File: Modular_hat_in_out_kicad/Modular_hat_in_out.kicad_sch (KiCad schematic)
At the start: 35 parts, among them J1 Raspberry_Pi_2_3, U1 MCP3008, U2 LM324, U3 MCP3008, U4 MCP4728

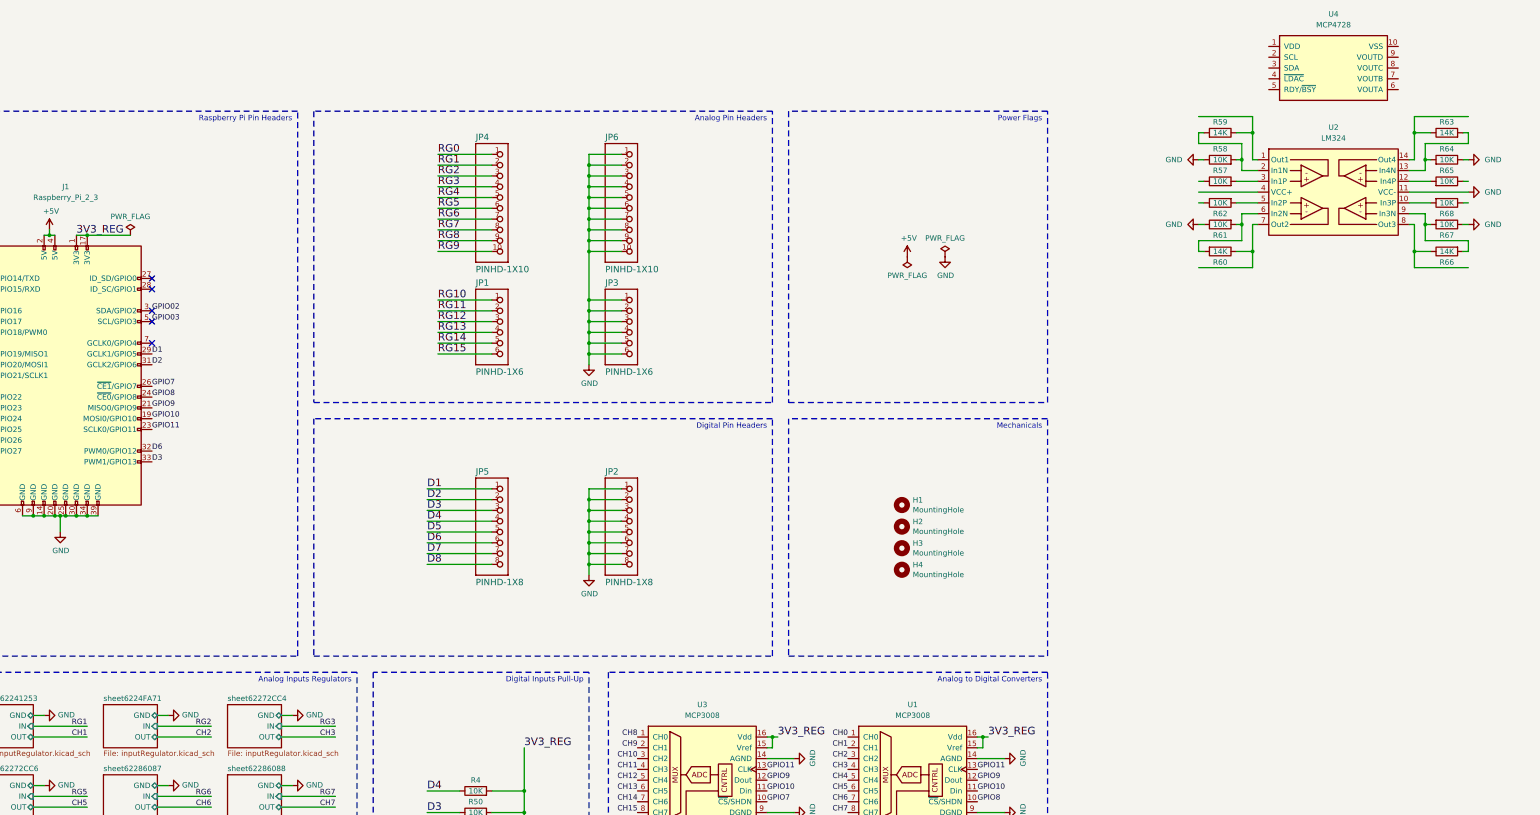
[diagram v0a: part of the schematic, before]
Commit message: [ADD] Connections and update configuration resistors
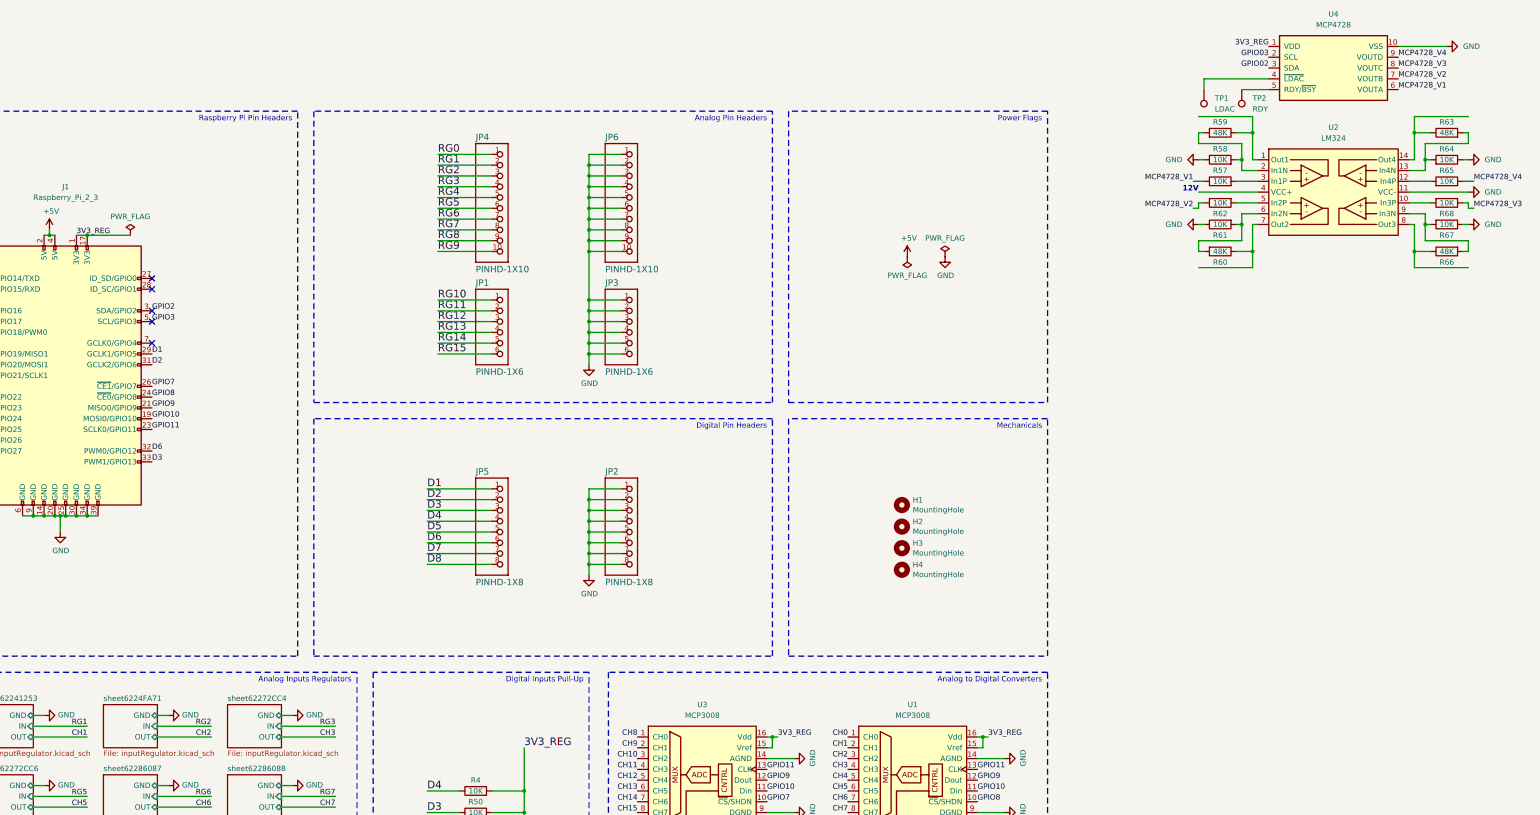
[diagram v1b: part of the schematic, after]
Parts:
- added TP1: LDAC, symbol Modular Shield:TestPoint
- added TP2: RDY, symbol Modular Shield:TestPoint
- R59, R60, R63, R66: value 14K -> 48K; symbol Modular Shield:R 14K -> Modular Shield:R 48K; LCSC C2930066 -> C227922
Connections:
- net 3V3_REG: now also U4.1 (VDD)
- net GND: now also U4.10 (VSS)
- net GPIO02: now also U4.3 (SDA); no longer J1.3 (SDA/GPIO2)
- net GPIO03: now also U4.2 (SCL); no longer J1.5 (SCL/GPIO3)
- net MCP4728_V3: now reaches R68.1
- net MCP4728_V3: now also U4.8 (VOUTC)
- net at U4.4 (~{LDAC}): now also TP1.1
- net at U4.5 (RDY/~{BSY}): now also TP2.1
- net MCP4728_V1: now reaches U4.6 (VOUTA)
- net MCP4728_V1: now also R57.1
- net MCP4728_V2: now reaches U4.7 (VOUTB)
- net MCP4728_V2: now also R62.1
- net MCP4728_V4: now reaches U4.9 (VOUTD)
- net MCP4728_V4: now also R65.1
- new net GPIO2: J1.3 (SDA/GPIO2)
- new net GPIO3: J1.5 (SCL/GPIO3)
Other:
- note added: "12V"

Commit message: [ADD] Update design and Schematics for 4 channels DAC seems OK
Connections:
- net OP0: now reaches R59.2, U2.1 (Out1)
- net OP4: now reaches R63.2, U2.14 (Out4)
- net OP3: now reaches R66.2, U2.8 (Out3)
- net OP2: now reaches R60.2, U2.7 (Out2)
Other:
- removed sheet sheet62241253
- removed sheet sheet6224FA71
- removed sheet sheet62272CC4
- removed sheet sheet62272CC5
- removed sheet sheet62272CC6
- removed sheet sheet62286087
- removed sheet sheet62286088
- removed sheet sheet62286089
- removed sheet sheet6229E4C7
- removed sheet sheet6229E4C8
- removed sheet sheet6229E4C9
- removed sheet sheet6229E4CA
- removed sheet sheet6229E4CB
- removed sheet sheet6229E4CC
- removed sheet sheet622B5734
- added sheet outputProtection (outputProtection.kicad_sch)
- moved on the sheet: TP1, TP2, U4

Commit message: [ADD] Schematics in progress
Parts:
- added C1, C3: 0.1uF, symbol Modular Shield:C
- added C2, C4: 10uF, symbol Modular Shield:C
- added JP7, JP8: PINHD-1X8, Modular Shield:1X08-BIG, symbol Modular Shield:PINHD-1X8
- added R73, R74, R75, R77, R78, R79, R80, R82, R84, R85, R86, R87: 10K, Modular Shield:R_0603_1608Metric, symbol Modular Shield:R 10K
- added R76, R81, R83, R88: 48K, Modular Shield:R_0603_1608Metric, symbol Modular Shield:R 48K
- added TP3: LDAC, symbol Modular Shield:TestPoint
- added TP4, TP5, TP6: RDY, symbol Modular Shield:TestPoint
- added U5: MCP4728, Package_SO:MSOP-10_3x3mm_P0.5mm, symbol Modular Shield:MCP4728
- added U6: LM324, symbol Modular Shield:LM324
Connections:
- net +5V: now also U4.1 (VDD), C1.1, C2.1, C3.1, C4.1, U5.1 (VDD)
- net 3V3_REG: now also R73.2, R74.1, R75.1, R82.2; no longer U4.1 (VDD)
- net GND: now also C1.2, C2.2, C3.2, C4.2, JP8.1, JP8.2, JP8.3, JP8.4, JP8.5, JP8.6, JP8.7, JP8.8, R77.1, R80.1, R84.1, R87.1, TP5.1, TP6.1, U5.10 (VSS), U6.11 (VCC-)
- net GPIO02: now also R74.2, R75.2, U5.3 (SDA)
- net GPIO03: now also R73.1, R82.1, U5.2 (SCL)
- net MCP4728_V1 renamed MCP4728_V0_1
- net MCP4728_V2 renamed MCP4728_V0_2
- net MCP4728_V3 renamed MCP4728_V0_3
- net MCP4728_V4 renamed MCP4728_V0_4
- net OP0 renamed OP0_0
- net OP2 renamed OP0_2
- net OP3 renamed OP0_3
- net OP4 renamed OP0_4
- new net: R85.2, U6.12 (In4P)
- new net: R76.1, R77.2, U6.2 (In1N)
- new net: TP4.1, U5.5 (RDY/~{BSY})
- new net: TP3.1, U5.4 (~{LDAC})
- new net: R78.2, U6.3 (In1P)
- new net: R86.2, U6.10 (In3P)
- new net: R79.2, U6.5 (In2P)
- new net: R83.1, R84.2, U6.13 (In4N)
- new net: R80.2, R81.1, U6.6 (In2N)
- new net: R87.2, R88.1, U6.9 (In3N)
- new net A0: JP7.1
- new net A1: JP7.2
- new net A2: JP7.3
- new net A3: JP7.4
- new net A4: JP7.5
- new net A5: JP7.6
- new net A6: JP7.7
- new net A7: JP7.8
- new net MCP4728_V1_1: R78.1, U5.6 (VOUTA)
- new net MCP4728_V1_2: R79.1, U5.7 (VOUTB)
- new net MCP4728_V1_3: R86.1, U5.8 (VOUTC)
- new net MCP4728_V1_4: R85.1, U5.9 (VOUTD)
- new net OP1_0: R76.2, U6.1 (Out1)
- new net OP1_2: R81.2, U6.7 (Out2)
- new net OP1_3: R88.2, U6.8 (Out3)
- new net OP1_4: R83.2, U6.14 (Out4)
- no-connect marks 15 -> 13
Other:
- added sheet outputProtection1 (outputProtection.kicad_sch)
- added sheet outputProtection2 (outputProtection.kicad_sch)
- added sheet outputProtection3 (outputProtection.kicad_sch)
- added sheet outputProtection4 (outputProtection.kicad_sch)
- note added: "Analog In Pin Headers"
- note added: "Analog Out Pin Headers"
- note added: "Analog Outputs Protections"
- note added: "Digital to Analog Converters"
- note added: "Operational Amplifiers"
- note added: "Test Points"
- note removed: "Analog Pin Headers"
- moved on the sheet: H1, H2, H3, H4, JP1, JP2, JP3, JP4, JP5, JP6, R4, R50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

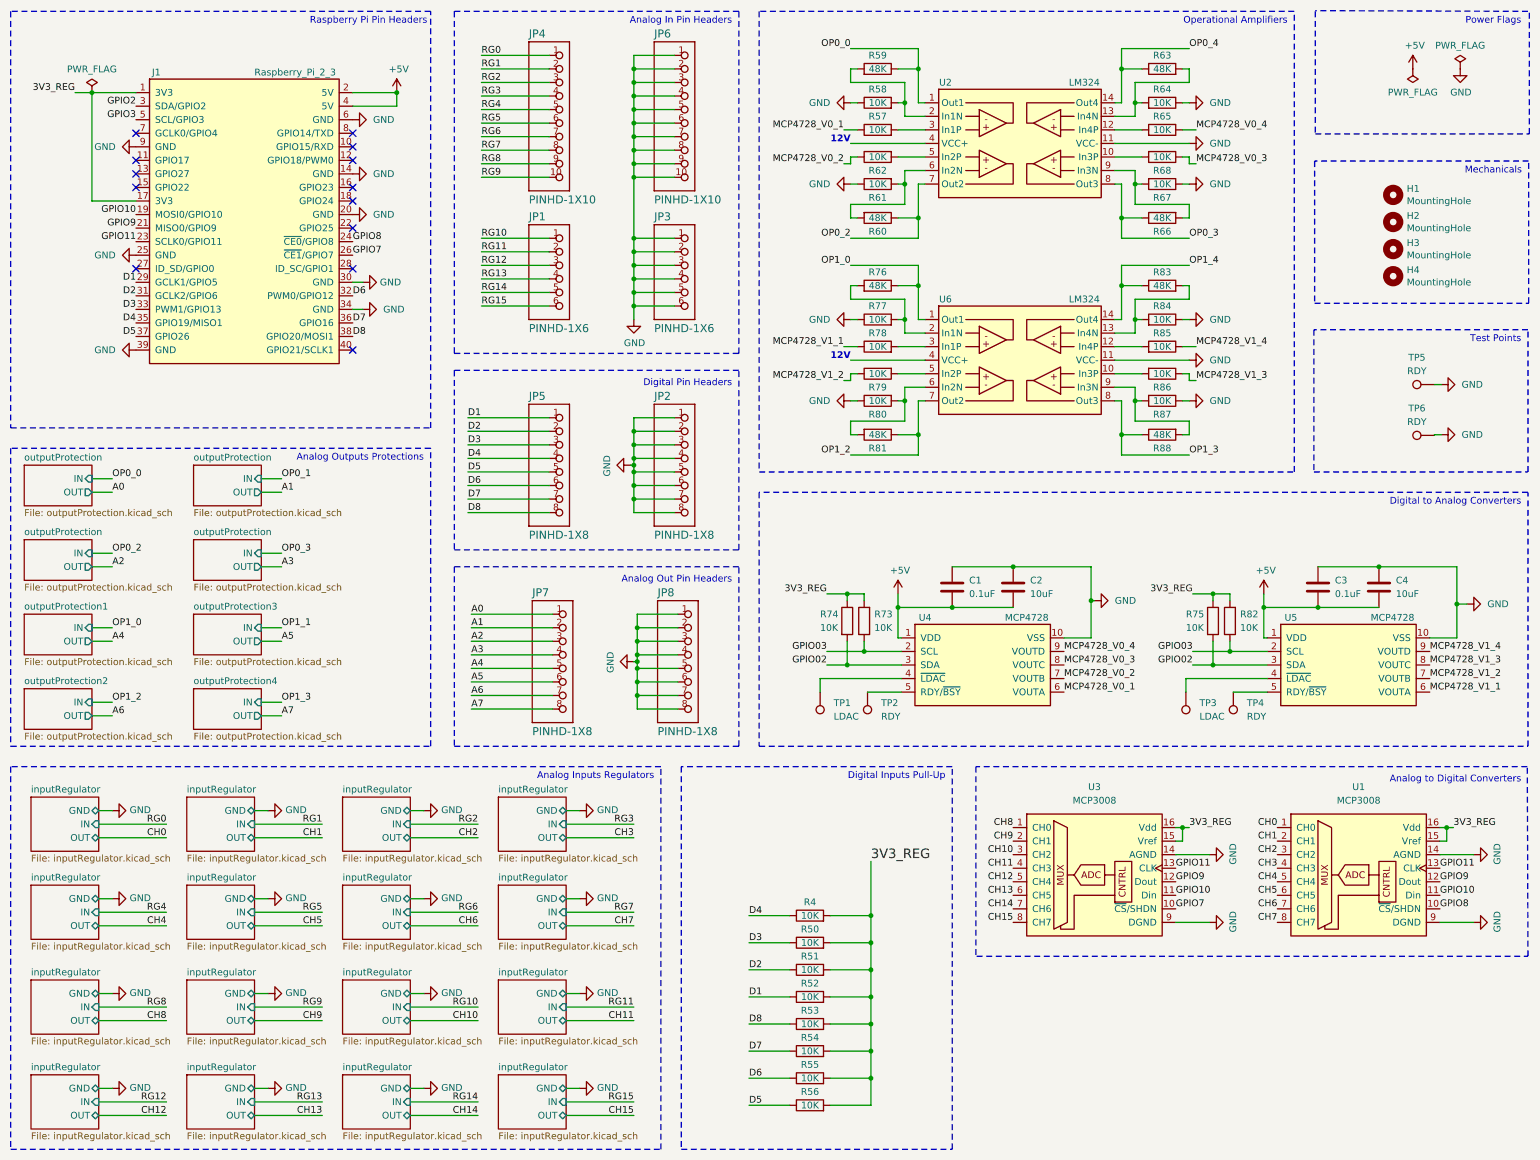
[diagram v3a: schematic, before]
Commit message: [ERC] Major problems fixed
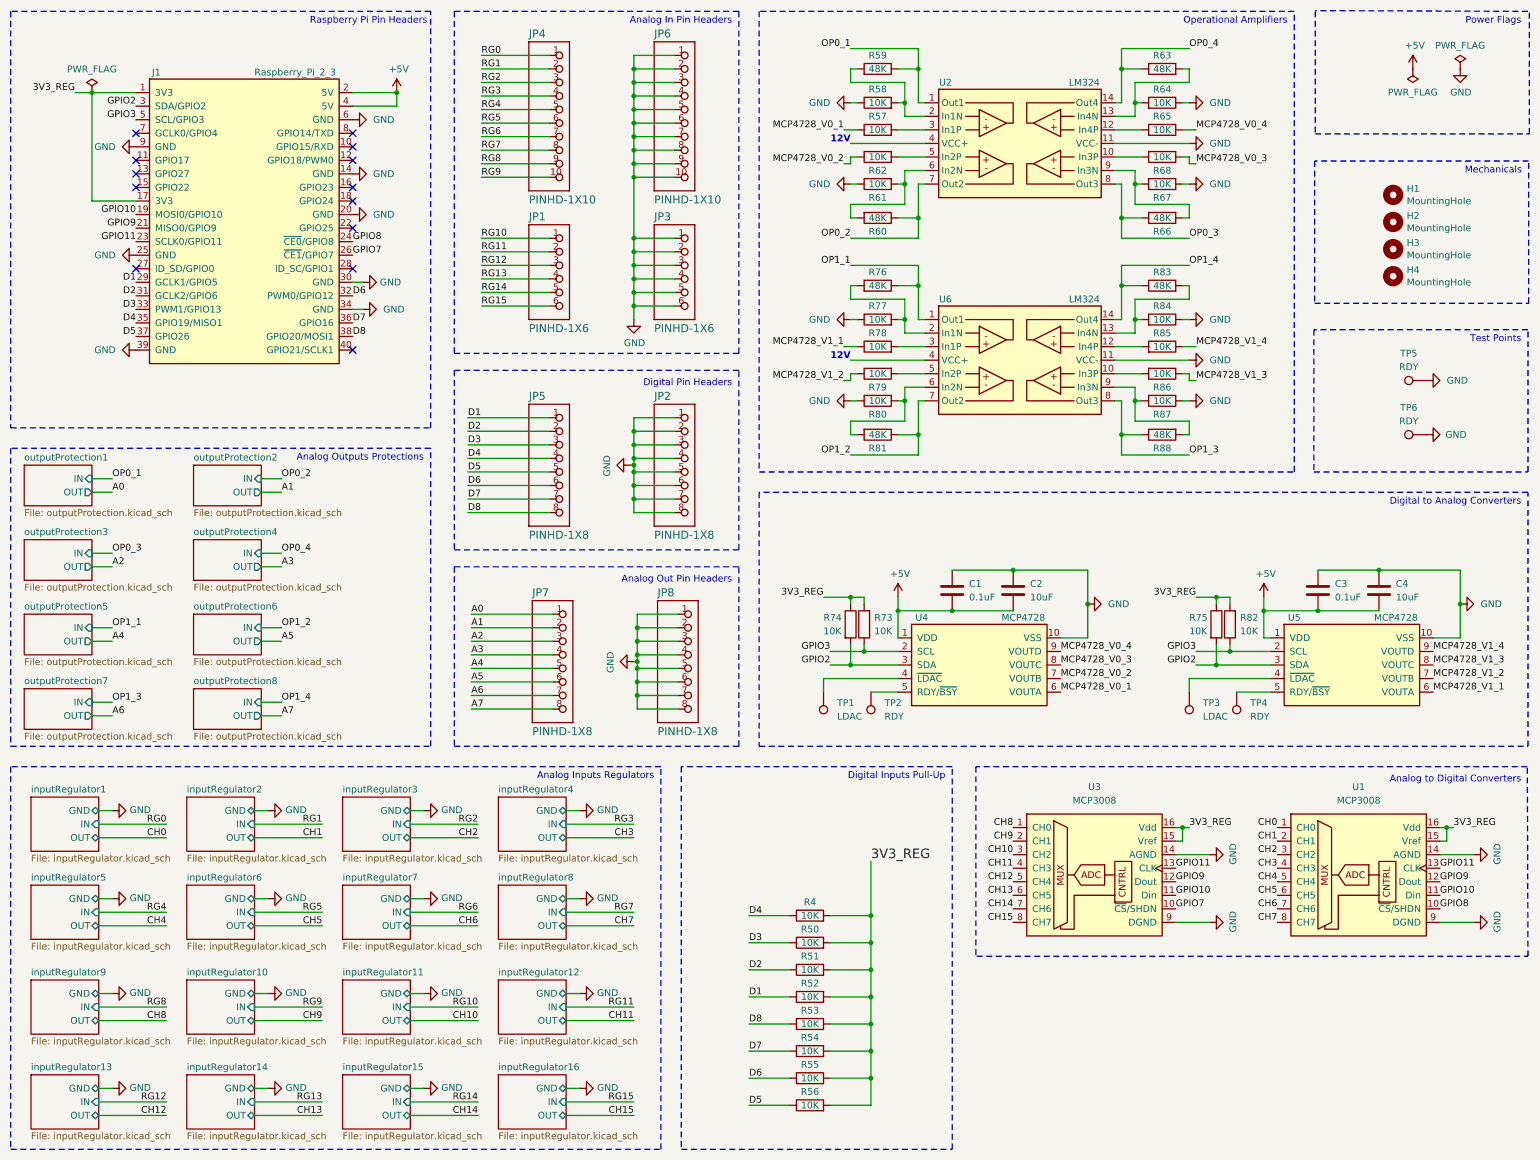
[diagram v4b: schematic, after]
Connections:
- net GPIO02 is gone; now on net GPIO2: R74.2, R75.2, U4.3 (SDA), U5.3 (SDA)
- net GPIO03 is gone; now on net GPIO3: R73.1, R82.1, U4.2 (SCL), U5.2 (SCL)
- net OP0_0 is gone; now on net OP0_1: R59.2, U2.1 (Out1)
- net OP1_0 is gone; now on net OP1_1: R76.2, U6.1 (Out1)
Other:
- sheet inputRegulator renamed inputRegulator16
- removed sheet outputProtection
- added sheet inputRegulator1 (inputRegulator.kicad_sch)
- added sheet inputRegulator10 (inputRegulator.kicad_sch)
- added sheet inputRegulator11 (inputRegulator.kicad_sch)
- added sheet inputRegulator12 (inputRegulator.kicad_sch)
- added sheet inputRegulator13 (inputRegulator.kicad_sch)
- added sheet inputRegulator14 (inputRegulator.kicad_sch)
- added sheet inputRegulator15 (inputRegulator.kicad_sch)
- added sheet inputRegulator2 (inputRegulator.kicad_sch)
- added sheet inputRegulator3 (inputRegulator.kicad_sch)
- added sheet inputRegulator4 (inputRegulator.kicad_sch)
- added sheet inputRegulator5 (inputRegulator.kicad_sch)
- added sheet inputRegulator6 (inputRegulator.kicad_sch)
- added sheet inputRegulator7 (inputRegulator.kicad_sch)
- added sheet inputRegulator8 (inputRegulator.kicad_sch)
- added sheet inputRegulator9 (inputRegulator.kicad_sch)
- added sheet outputProtection5 (outputProtection.kicad_sch)
- added sheet outputProtection6 (outputProtection.kicad_sch)
- added sheet outputProtection7 (outputProtection.kicad_sch)
- added sheet outputProtection8 (outputProtection.kicad_sch)
- moved on the sheet: C1, C2, C3, C4, R73, R74, R75, R82, TP1, TP2, TP3, TP4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
